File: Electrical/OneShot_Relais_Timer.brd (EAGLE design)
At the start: 65 x 63 mm, 15 parts, among them IC2 ATTINY204SOIC14, K1 RE030012, T1 BC847, X1 MKDSN1,5/3-5,08

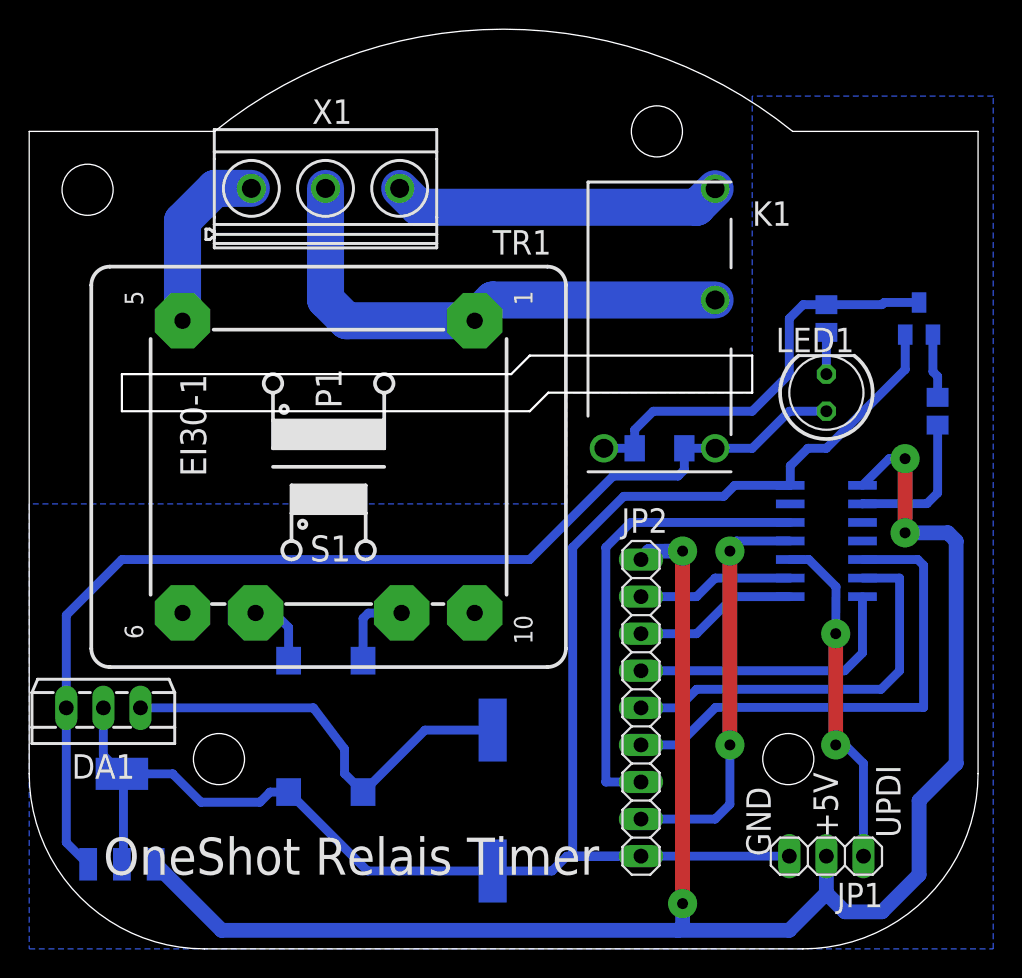
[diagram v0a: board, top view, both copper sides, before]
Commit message: Moved 12V regulator to other side, improved texts, improved UI PCB (increased vias and traces)
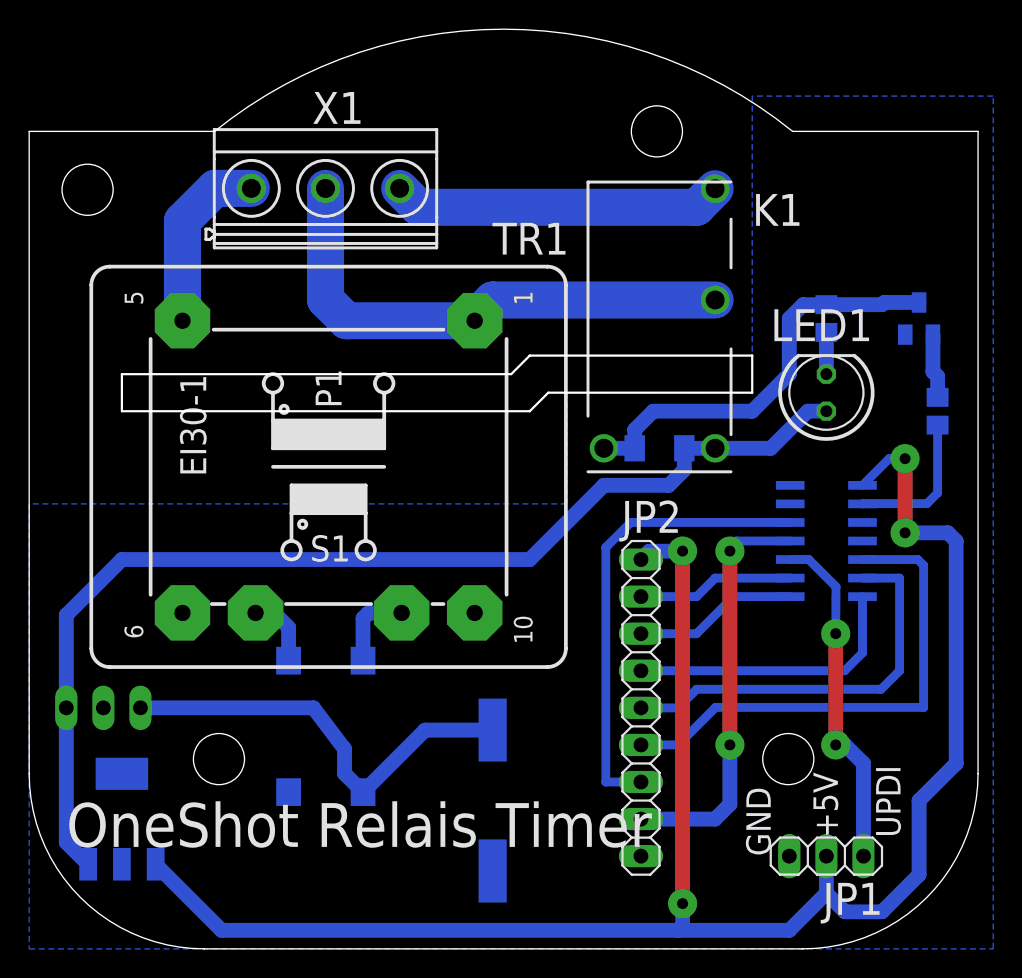
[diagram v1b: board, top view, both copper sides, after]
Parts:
- moved DA1 5.08 mm to (5.08, 19.1), flipped to the bottom, turned to 0 degrees
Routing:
- net GND: track 117.6 -> 0.39 mm

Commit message: Small adaptions to PCBs, schematics, and mechanical components
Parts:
- R1: value 10k -> 1k
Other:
- board text added: "L"
- board text added: "L_out"
- board text added: "N"
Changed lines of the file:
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@@
 <text x="50.8" y="6.35" size="1.6764" layer="25" ratio="15" rot="R90">GND</text>
 <text x="55.4" y="7.62" size="1.6764" layer="25" ratio="15" rot="R90">+5V</text>
+<text x="8.89" y="50.8" size="3" layer="25" ratio="15">N</text>
+<text x="28.575" y="51.435" size="3" layer="25" ratio="15">L_out</text>
+<text x="19.685" y="56.515" size="3" layer="25" ratio="15">L</text>
 </plain>
 <attributes>
@@
 </autorouter>
 <elements>
-<element name="R1" library="OwnDevices" library_urn="urn:adsk.eagle:library:19498084" package="R0805" package3d_urn="urn:adsk.eagle:package:23553/2" value="10k" x="62.23" y="36.83" smashed="yes" rot="MR90">
+<element name="R1" library="OwnDevices" library_urn="urn:adsk.eagle:library:19498084" package="R0805" package3d_urn="urn:adsk.eagle:package:23553/2" value="1k" x="62.23" y="36.83" smashed="yes" rot="MR90">
 <attribute name="NAME" x="60.325" y="36.83" size="2.1844" layer="26" ratio="15" rot="MR0"/>
 <attribute name="POPULARITY" value="86" x="62.23" y="36.83" size="1.778" layer="28" rot="MR90" display="off"/>
@@
 </element>
 <element name="X1" library="OwnDevices" library_urn="urn:adsk.eagle:library:19498084" package="MKDSN1,5/3-5,08" package3d_urn="urn:adsk.eagle:package:37656663/2" value="MKDSN1,5/3-5,08" x="22.86" y="52.07" smashed="yes">
-<attribute name="NAME" x="19.3789" y="56.515" size="2.1844" layer="25" ratio="15"/>
+<attribute name="NAME" x="25.0939" y="57.15" size="2.1844" layer="25" ratio="15"/>
 <attribute name="POPULARITY" value="0" x="22.86" y="52.07" size="1.778" layer="27" display="off"/>
 <attribute name="VALUE" x="26.67" y="56.515" size="1.27" layer="27"/>
